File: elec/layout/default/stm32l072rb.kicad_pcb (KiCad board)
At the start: 2 copper layers, 40 x 40 mm, 0 parts

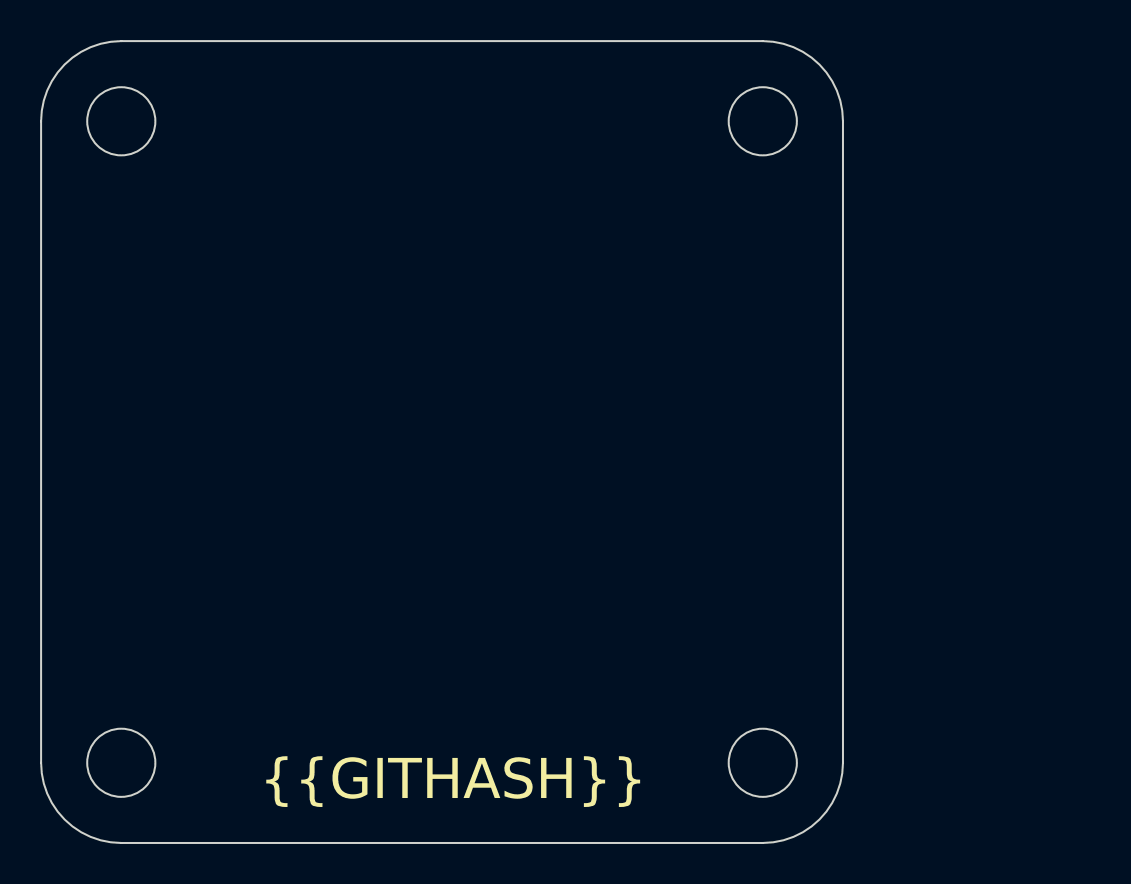
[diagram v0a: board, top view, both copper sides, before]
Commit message: added proper power managment
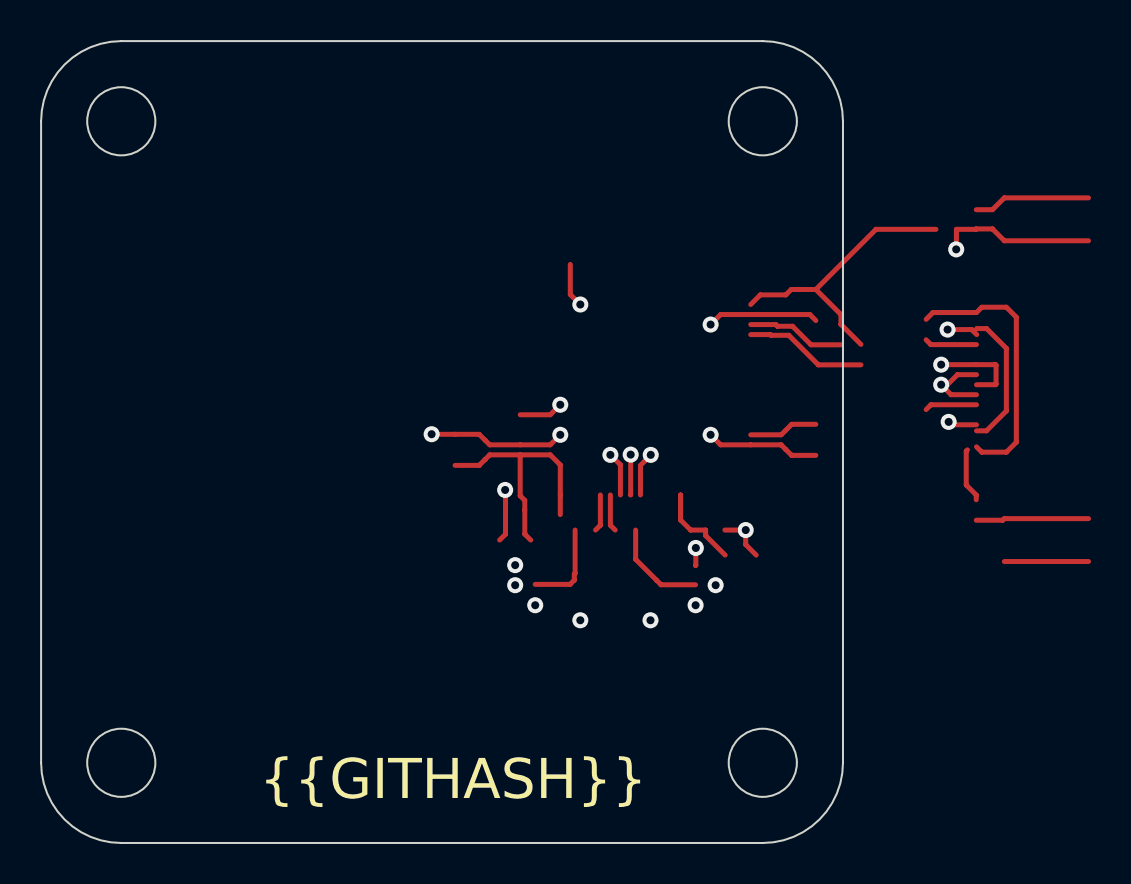
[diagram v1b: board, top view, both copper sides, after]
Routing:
- net 1: track 0.00 -> 48.4 mm, vias 0 -> 15
- net 16: track 0.00 -> 34.8 mm
- net 3: track 0.00 -> 10.1 mm, vias 0 -> 2
- net 8: track 0.00 -> 9.92 mm, vias 0 -> 2
- net 4: track 0.00 -> 7.84 mm, vias 0 -> 1
- net 5: track 0.00 -> 6.83 mm
- net 15: track 0.00 -> 6.13 mm
- net 7: track 0.00 -> 5.41 mm
- net 17: track 0.00 -> 4.92 mm
- net 12: track 0.00 -> 4.68 mm, vias 0 -> 1
- net 14: track 0.00 -> 4.55 mm
- net 13: track 0.00 -> 3.94 mm, vias 0 -> 1
- net 11: track 0.00 -> 2.61 mm
- net 10: track 0.00 -> 2.61 mm
- net 2: track 0.00 -> 2.21 mm, vias 0 -> 1
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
